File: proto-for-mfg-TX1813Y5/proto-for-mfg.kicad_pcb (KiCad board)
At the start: 2 copper layers, 191.4 x 111.9 mm, 57 parts, among them J1 Conn_01x03_Pin

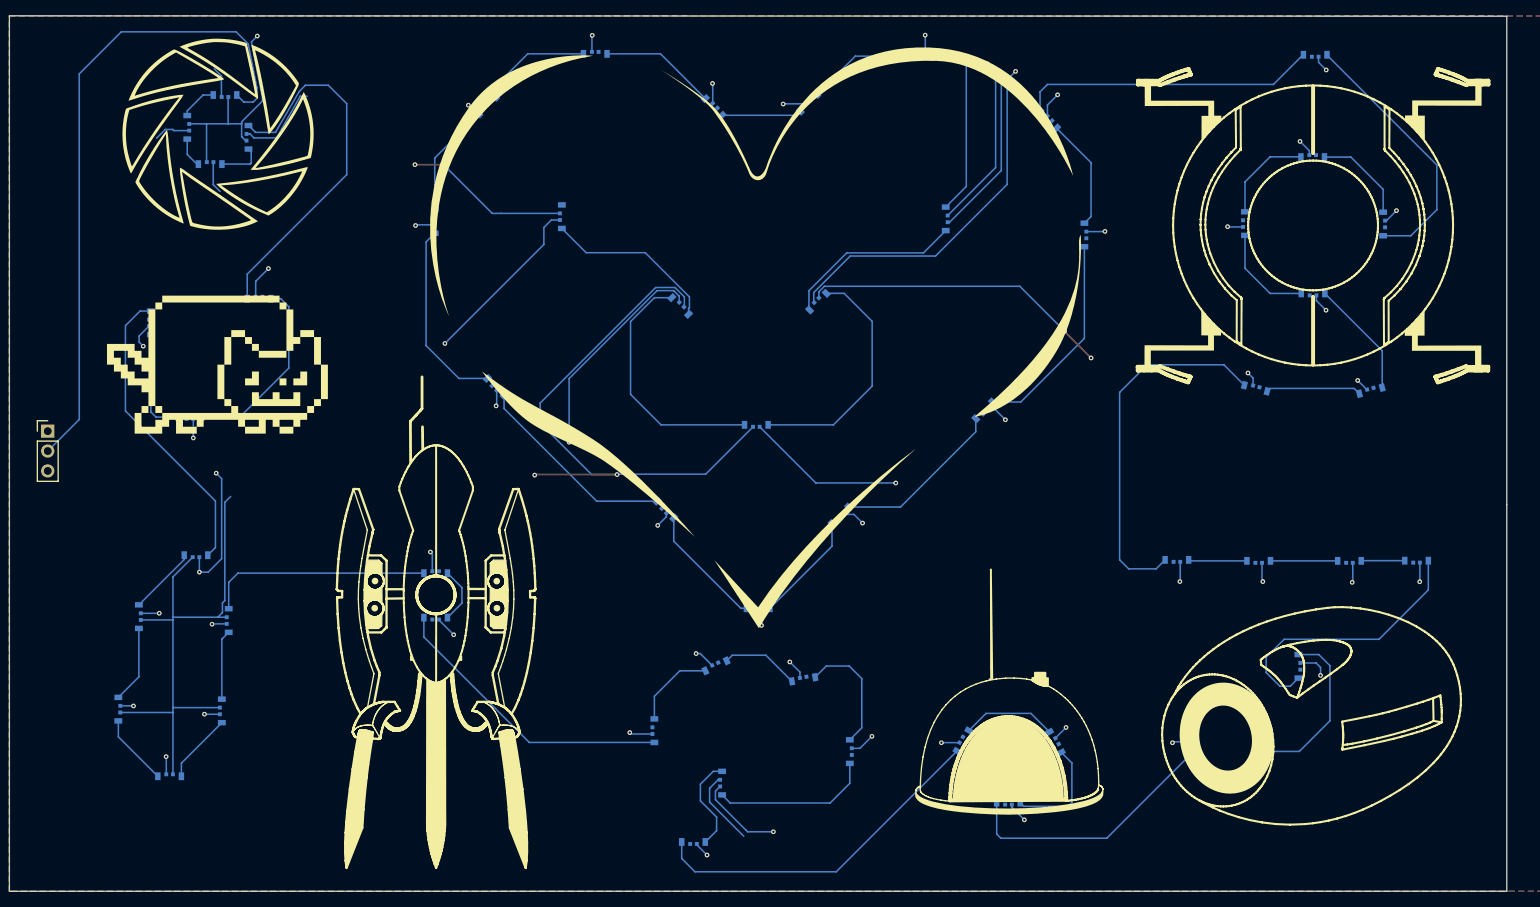
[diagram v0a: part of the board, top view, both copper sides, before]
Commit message: move over to new LED and fix design
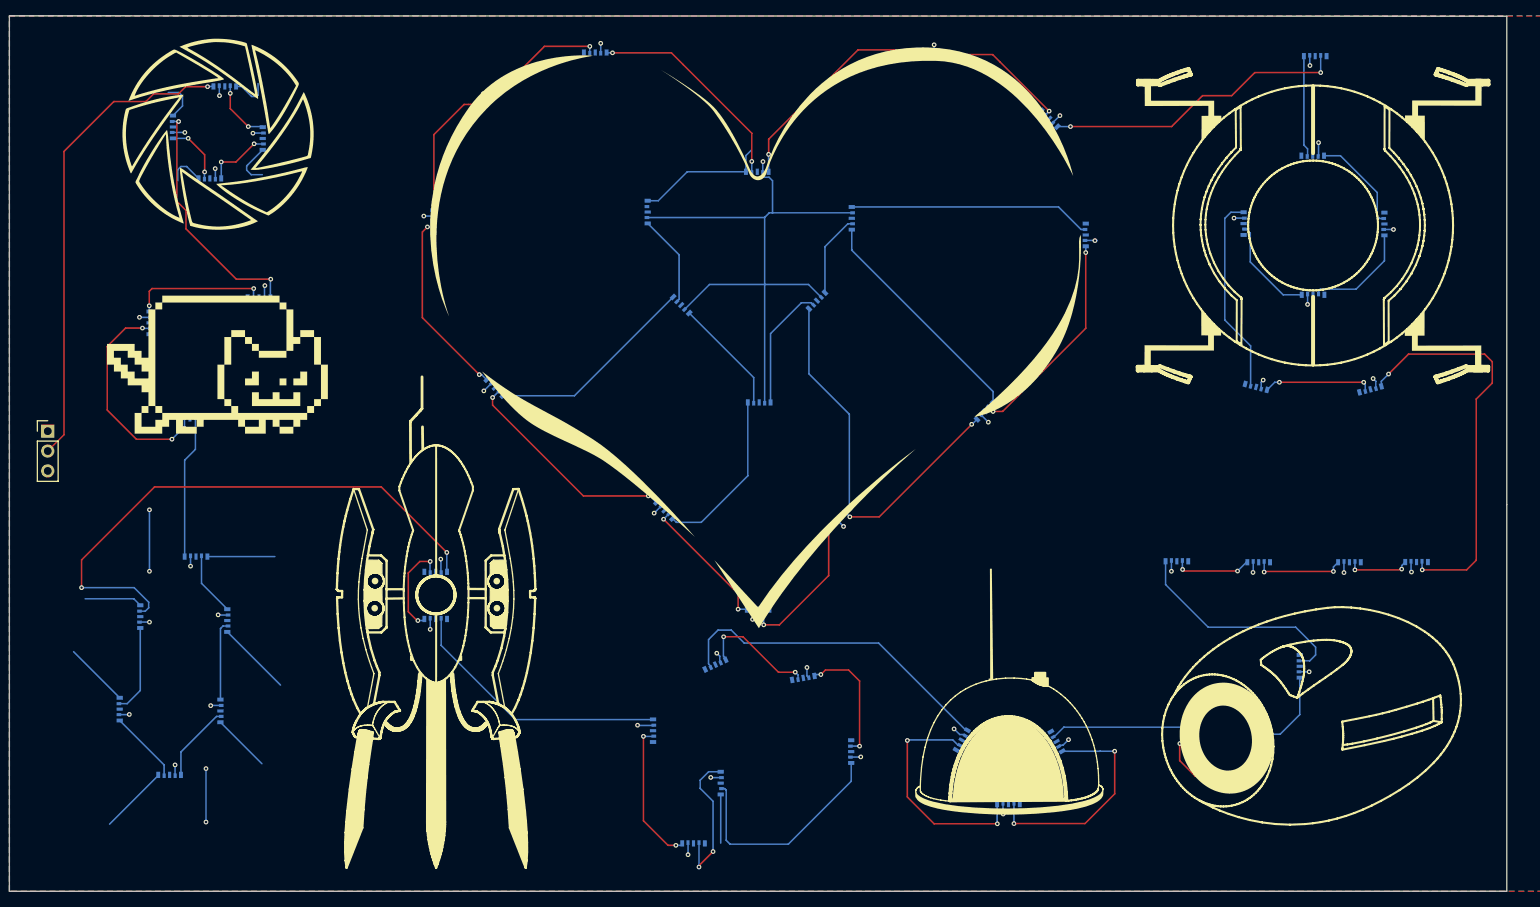
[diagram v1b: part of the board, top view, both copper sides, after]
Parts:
- removed the U50 at (124.6, 49.0)
- U1, U11, U14, U15, U16, U19, U22, U25, U26, U27, U3, U38, U39, U45, U5, U8: footprint LED_SMD:LED-SMD_4P_SK6812D-EC3210R -> LED_SMD:LED-SMD_5P-L3.2-W1.4_TX1813Y5
- U10: renamed from U12; footprint LED_SMD:LED-SMD_4P_SK6812D-EC3210R -> LED_SMD:LED-SMD_5P-L3.2-W1.4_TX1813Y5
- U12: renamed from U10; footprint LED_SMD:LED-SMD_4P_SK6812D-EC3210R -> LED_SMD:LED-SMD_5P-L3.2-W1.4_TX1813Y5
- U13: renamed from U9; footprint LED_SMD:LED-SMD_4P_SK6812D-EC3210R -> LED_SMD:LED-SMD_5P-L3.2-W1.4_TX1813Y5
- U17: renamed from U21; footprint LED_SMD:LED-SMD_4P_SK6812D-EC3210R -> LED_SMD:LED-SMD_5P-L3.2-W1.4_TX1813Y5
- U18: renamed from U20; footprint LED_SMD:LED-SMD_4P_SK6812D-EC3210R -> LED_SMD:LED-SMD_5P-L3.2-W1.4_TX1813Y5
- U2: renamed from U4; footprint LED_SMD:LED-SMD_4P_SK6812D-EC3210R -> LED_SMD:LED-SMD_5P-L3.2-W1.4_TX1813Y5
- U20: renamed from U18; footprint LED_SMD:LED-SMD_4P_SK6812D-EC3210R -> LED_SMD:LED-SMD_5P-L3.2-W1.4_TX1813Y5
- U21: renamed from U17; footprint LED_SMD:LED-SMD_4P_SK6812D-EC3210R -> LED_SMD:LED-SMD_5P-L3.2-W1.4_TX1813Y5
- U23: renamed from U24; footprint LED_SMD:LED-SMD_4P_SK6812D-EC3210R -> LED_SMD:LED-SMD_5P-L3.2-W1.4_TX1813Y5
- U24: renamed from U23; footprint LED_SMD:LED-SMD_4P_SK6812D-EC3210R -> LED_SMD:LED-SMD_5P-L3.2-W1.4_TX1813Y5
- U28: renamed from U31; footprint LED_SMD:LED-SMD_4P_SK6812D-EC3210R -> LED_SMD:LED-SMD_5P-L3.2-W1.4_TX1813Y5
- U29: renamed from U30; footprint LED_SMD:LED-SMD_4P_SK6812D-EC3210R -> LED_SMD:LED-SMD_5P-L3.2-W1.4_TX1813Y5
- U30: renamed from U29; footprint LED_SMD:LED-SMD_4P_SK6812D-EC3210R -> LED_SMD:LED-SMD_5P-L3.2-W1.4_TX1813Y5
- U31: renamed from U28; footprint LED_SMD:LED-SMD_4P_SK6812D-EC3210R -> LED_SMD:LED-SMD_5P-L3.2-W1.4_TX1813Y5
- U32: renamed from U33; footprint LED_SMD:LED-SMD_4P_SK6812D-EC3210R -> LED_SMD:LED-SMD_5P-L3.2-W1.4_TX1813Y5
- U33: renamed from U32; footprint LED_SMD:LED-SMD_4P_SK6812D-EC3210R -> LED_SMD:LED-SMD_5P-L3.2-W1.4_TX1813Y5
- U34: renamed from U35; footprint LED_SMD:LED-SMD_4P_SK6812D-EC3210R -> LED_SMD:LED-SMD_5P-L3.2-W1.4_TX1813Y5
- U35: renamed from U34; footprint LED_SMD:LED-SMD_4P_SK6812D-EC3210R -> LED_SMD:LED-SMD_5P-L3.2-W1.4_TX1813Y5
- U36: renamed from U37; footprint LED_SMD:LED-SMD_4P_SK6812D-EC3210R -> LED_SMD:LED-SMD_5P-L3.2-W1.4_TX1813Y5
- U37: renamed from U36; footprint LED_SMD:LED-SMD_4P_SK6812D-EC3210R -> LED_SMD:LED-SMD_5P-L3.2-W1.4_TX1813Y5
- U4: renamed from U2; footprint LED_SMD:LED-SMD_4P_SK6812D-EC3210R -> LED_SMD:LED-SMD_5P-L3.2-W1.4_TX1813Y5
- U40: renamed from U51; footprint LED_SMD:LED-SMD_4P_SK6812D-EC3210R -> LED_SMD:LED-SMD_5P-L3.2-W1.4_TX1813Y5
- U41: renamed from U49; footprint LED_SMD:LED-SMD_4P_SK6812D-EC3210R -> LED_SMD:LED-SMD_5P-L3.2-W1.4_TX1813Y5
- U42: renamed from U48; footprint LED_SMD:LED-SMD_4P_SK6812D-EC3210R -> LED_SMD:LED-SMD_5P-L3.2-W1.4_TX1813Y5
- U43: renamed from U47; footprint LED_SMD:LED-SMD_4P_SK6812D-EC3210R -> LED_SMD:LED-SMD_5P-L3.2-W1.4_TX1813Y5
- U44: renamed from U46; footprint LED_SMD:LED-SMD_4P_SK6812D-EC3210R -> LED_SMD:LED-SMD_5P-L3.2-W1.4_TX1813Y5
- U46: renamed from U44; footprint LED_SMD:LED-SMD_4P_SK6812D-EC3210R -> LED_SMD:LED-SMD_5P-L3.2-W1.4_TX1813Y5
- U47: renamed from U43; footprint LED_SMD:LED-SMD_4P_SK6812D-EC3210R -> LED_SMD:LED-SMD_5P-L3.2-W1.4_TX1813Y5
- U48: renamed from U42; footprint LED_SMD:LED-SMD_4P_SK6812D-EC3210R -> LED_SMD:LED-SMD_5P-L3.2-W1.4_TX1813Y5
- U49: renamed from U41; footprint LED_SMD:LED-SMD_4P_SK6812D-EC3210R -> LED_SMD:LED-SMD_5P-L3.2-W1.4_TX1813Y5
- U50: renamed from U40; footprint LED_SMD:LED-SMD_4P_SK6812D-EC3210R -> LED_SMD:LED-SMD_5P-L3.2-W1.4_TX1813Y5
- U51: renamed from U52; footprint LED_SMD:LED-SMD_4P_SK6812D-EC3210R -> LED_SMD:LED-SMD_5P-L3.2-W1.4_TX1813Y5
- U52: renamed from U53; footprint LED_SMD:LED-SMD_4P_SK6812D-EC3210R -> LED_SMD:LED-SMD_5P-L3.2-W1.4_TX1813Y5
- U53: renamed from U54; footprint LED_SMD:LED-SMD_4P_SK6812D-EC3210R -> LED_SMD:LED-SMD_5P-L3.2-W1.4_TX1813Y5
- U54: renamed from U55; footprint LED_SMD:LED-SMD_4P_SK6812D-EC3210R -> LED_SMD:LED-SMD_5P-L3.2-W1.4_TX1813Y5
- U55: renamed from U56; footprint LED_SMD:LED-SMD_4P_SK6812D-EC3210R -> LED_SMD:LED-SMD_5P-L3.2-W1.4_TX1813Y5
- U6: renamed from U7; footprint LED_SMD:LED-SMD_4P_SK6812D-EC3210R -> LED_SMD:LED-SMD_5P-L3.2-W1.4_TX1813Y5
- U7: renamed from U6; footprint LED_SMD:LED-SMD_4P_SK6812D-EC3210R -> LED_SMD:LED-SMD_5P-L3.2-W1.4_TX1813Y5
- U9: renamed from U13; footprint LED_SMD:LED-SMD_4P_SK6812D-EC3210R -> LED_SMD:LED-SMD_5P-L3.2-W1.4_TX1813Y5
- moved U51 12.1 mm to (130.3, 63.9)
- moved U55 11.1 mm to (104.1, 63.1)
- moved U41 10.0 mm to (118.1, 58.0), turned to 0 degrees
- moved U53 2.96 mm to (118.4, 87.4)
- moved U3 2.01 mm to (48.2, 58.8), turned to 0 degrees
- moved U4 2.01 mm to (43.4, 52.2), turned to -90 degrees
- moved U2 2.00 mm to (55.0, 53.7), turned to 90 degrees
- moved U1 1.27 mm to (50.1, 47.0), turned to 180 degrees
- turned U10 to 90 degrees
- turned U11 to 0 degrees
- turned U12 to -90 degrees
- turned U13 to -90 degrees
- turned U14 to 0 degrees
- turned U15 to 180 degrees
- turned U16 to 90 degrees
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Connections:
- U1 pad 1: GND -> Net-(J1-Pin_2)
- U1 pad 2: Net-(U1-DOUT) -> +3V3
- U1 pad 3: Net-(J1-Pin_2) -> unconnected-(U1-FDIN-Pad3)
- U1 pad 4: +3V3 -> Net-(U1-DO)
- U10 pad 1: GND -> Net-(U10-DIN)
- U10 pad 2: Net-(U12-DOUT) -> +3V3
- U10 pad 3: Net-(U11-DOUT) -> unconnected-(U10-FDIN-Pad3)
- U10 pad 4: +3V3 -> Net-(U10-DO)
- U11 pad 1: GND -> Net-(U10-DO)
- U11 pad 2: Net-(U11-DOUT) -> +3V3
- U11 pad 3: Net-(U10-DOUT) -> unconnected-(U11-FDIN-Pad3)
- U11 pad 4: +3V3 -> Net-(U11-DO)
- U12 pad 1: GND -> Net-(U11-DO)
- U12 pad 2: Net-(U10-DOUT) -> +3V3
- U12 pad 3: Net-(U10-DIN) -> unconnected-(U12-FDIN-Pad3)
- U12 pad 4: +3V3 -> Net-(U12-DO)
- U13 pad 1: GND -> Net-(U12-DO)
- U13 pad 2: Net-(U10-DIN) -> +3V3
- U13 pad 3: Net-(U8-DOUT) -> unconnected-(U13-FDIN-Pad3)
- U13 pad 4: +3V3 -> Net-(U13-DO)
- U14 pad 1: GND -> Net-(U13-DO)
- U14 pad 2: Net-(U14-DOUT) -> +3V3
- U14 pad 3: Net-(U13-DOUT) -> unconnected-(U14-FDIN-Pad3)
- U14 pad 4: +3V3 -> Net-(U14-DO)
- U15 pad 1: GND -> Net-(U14-DO)
- U15 pad 2: Net-(U15-DOUT) -> +3V3
- U15 pad 3: Net-(U14-DOUT) -> unconnected-(U15-FDIN-Pad3)
- U15 pad 4: +3V3 -> Net-(U15-DO)
- U16 pad 1: GND -> Net-(U15-DO)
- U16 pad 2: Net-(U16-DOUT) -> +3V3
- U16 pad 3: Net-(U15-DOUT) -> unconnected-(U16-FDIN-Pad3)
- U16 pad 4: +3V3 -> Net-(U16-DO)
- U17 pad 1: GND -> Net-(U16-DO)
- U17 pad 2: Net-(U21-DOUT) -> +3V3
- U17 pad 3: Net-(U20-DOUT) -> unconnected-(U17-FDIN-Pad3)
- U17 pad 4: +3V3 -> Net-(U17-DO)
- U18 pad 1: GND -> Net-(U17-DO)
- U18 pad 2: Net-(U20-DOUT) -> +3V3
- U18 pad 3: Net-(U19-DOUT) -> unconnected-(U18-FDIN-Pad3)
- U18 pad 4: +3V3 -> Net-(U18-DO)
- U19 pad 1: GND -> Net-(U18-DO)
- U19 pad 2: Net-(U19-DOUT) -> +3V3
- U19 pad 3: Net-(U18-DOUT) -> unconnected-(U19-FDIN-Pad3)
- U19 pad 4: +3V3 -> Net-(U19-DO)
- U2 pad 1: GND -> Net-(U1-DO)
- U2 pad 2: Net-(U4-DOUT) -> +3V3
- U2 pad 3: Net-(U3-DOUT) -> unconnected-(U2-FDIN-Pad3)
- U2 pad 4: +3V3 -> Net-(U2-DO)
- U20 pad 1: GND -> Net-(U19-DO)
- U20 pad 2: Net-(U18-DOUT) -> +3V3
- U20 pad 3: Net-(U17-DOUT) -> unconnected-(U20-FDIN-Pad3)
- U20 pad 4: +3V3 -> Net-(U20-DO)
- U21 pad 1: GND -> Net-(U20-DO)
- U21 pad 2: Net-(U17-DOUT) -> +3V3
- U21 pad 3: Net-(U16-DOUT) -> unconnected-(U21-FDIN-Pad3)
- U21 pad 4: +3V3 -> Net-(U21-DO)
- U22 pad 1: GND -> Net-(U21-DO)
- U22 pad 2: Net-(U22-DOUT) -> +3V3
- U22 pad 3: Net-(U21-DOUT) -> unconnected-(U22-FDIN-Pad3)
- U22 pad 4: +3V3 -> Net-(U22-DO)
- U23 pad 1: GND -> Net-(U22-DO)
- U23 pad 2: Net-(U24-DOUT) -> +3V3
- U23 pad 3: Net-(U23-DOUT) -> unconnected-(U23-FDIN-Pad3)
- U23 pad 4: +3V3 -> Net-(U23-DO)
- U24 pad 1: GND -> Net-(U23-DO)
- U24 pad 2: Net-(U23-DOUT) -> +3V3
- U24 pad 3: Net-(U22-DOUT) -> unconnected-(U24-FDIN-Pad3)
- U24 pad 4: +3V3 -> Net-(U24-DO)
- U25 pad 1: GND -> Net-(U24-DO)
- U25 pad 2: Net-(U25-DOUT) -> +3V3
- U25 pad 3: Net-(U24-DOUT) -> unconnected-(U25-FDIN-Pad3)
- U25 pad 4: +3V3 -> Net-(U25-DO)
- U26 pad 1: GND -> Net-(U25-DO)
- U26 pad 2: Net-(U26-DOUT) -> +3V3
- U26 pad 3: Net-(U25-DOUT) -> unconnected-(U26-FDIN-Pad3)
- U26 pad 4: +3V3 -> Net-(U26-DO)
- U27 pad 1: GND -> Net-(U26-DO)
- U27 pad 2: Net-(U27-DOUT) -> +3V3
- U27 pad 3: Net-(U26-DOUT) -> unconnected-(U27-FDIN-Pad3)
- U27 pad 4: +3V3 -> Net-(U27-DO)
- U28 pad 1: GND -> Net-(U27-DO)
- U28 pad 2: Net-(U31-DOUT) -> +3V3
- U28 pad 3: Net-(U30-DOUT) -> unconnected-(U28-FDIN-Pad3)
- U28 pad 4: +3V3 -> Net-(U28-DO)
- U29 pad 1: GND -> Net-(U28-DO)
- U29 pad 2: Net-(U30-DOUT) -> +3V3
- U29 pad 3: Net-(U29-DOUT) -> unconnected-(U29-FDIN-Pad3)
- U29 pad 4: +3V3 -> Net-(U29-DO)
- U3 pad 1: GND -> Net-(U2-DO)
- U3 pad 2: Net-(U3-DOUT) -> +3V3
- U3 pad 3: Net-(U2-DOUT) -> unconnected-(U3-FDIN-Pad3)
- U3 pad 4: +3V3 -> Net-(U3-DO)
- U30 pad 1: GND -> Net-(U29-DO)
- U30 pad 2: Net-(U29-DOUT) -> +3V3
- U30 pad 3: Net-(U28-DOUT) -> unconnected-(U30-FDIN-Pad3)
- U30 pad 4: +3V3 -> Net-(U30-DO)
- U31 pad 1: GND -> Net-(U30-DO)
- U31 pad 2: Net-(U28-DOUT) -> +3V3
- U31 pad 3: Net-(U27-DOUT) -> unconnected-(U31-FDIN-Pad3)
- U31 pad 4: +3V3 -> Net-(U31-DO)
- U32 pad 1: GND -> Net-(U31-DO)
- U32 pad 2: Net-(U33-DOUT) -> +3V3
- U32 pad 3: Net-(U32-DOUT) -> unconnected-(U32-FDIN-Pad3)
- U32 pad 4: +3V3 -> Net-(U32-DO)
- U33 pad 1: GND -> Net-(U32-DO)
- U33 pad 2: Net-(U32-DOUT) -> +3V3
- U33 pad 3: Net-(U31-DOUT) -> unconnected-(U33-FDIN-Pad3)
- U33 pad 4: +3V3 -> Net-(U33-DO)
- U34 pad 1: GND -> Net-(U33-DO)
- U34 pad 2: Net-(U35-DOUT) -> +3V3
- U34 pad 3: Net-(U34-DOUT) -> unconnected-(U34-FDIN-Pad3)
- U34 pad 4: +3V3 -> Net-(U34-DO)
- U35 pad 1: GND -> Net-(U34-DO)
- U35 pad 2: Net-(U34-DOUT) -> +3V3
- U35 pad 3: Net-(U33-DOUT) -> unconnected-(U35-FDIN-Pad3)
- U35 pad 4: +3V3 -> Net-(U35-DO)
- U36 pad 1: GND -> Net-(U35-DO)
- U36 pad 2: Net-(U37-DOUT) -> +3V3
- U36 pad 3: Net-(U36-DOUT) -> unconnected-(U36-FDIN-Pad3)
- U36 pad 4: +3V3 -> Net-(U36-DO)
- U37 pad 1: GND -> Net-(U36-DO)
- U37 pad 2: Net-(U36-DOUT) -> +3V3
- U37 pad 3: Net-(U35-DOUT) -> unconnected-(U37-FDIN-Pad3)
- U37 pad 4: +3V3 -> Net-(U37-DO)
- U38 pad 1: GND -> Net-(U37-DO)
- U38 pad 2: Net-(U38-DOUT) -> +3V3
- U38 pad 3: Net-(U37-DOUT) -> unconnected-(U38-FDIN-Pad3)
- U38 pad 4: +3V3 -> Net-(U38-DO)
- U39 pad 1: GND -> Net-(U38-DO)
- U39 pad 2: Net-(U39-DOUT) -> +3V3
- U39 pad 3: Net-(U38-DOUT) -> unconnected-(U39-FDIN-Pad3)
- U39 pad 4: +3V3 -> Net-(U39-DO)
- U4 pad 1: GND -> Net-(U3-DO)
- U4 pad 2: Net-(U2-DOUT) -> +3V3
- U4 pad 3: Net-(U1-DOUT) -> unconnected-(U4-FDIN-Pad3)
- U4 pad 4: +3V3 -> Net-(U4-DO)
- U40 pad 1: GND -> Net-(U39-DO)
- U40 pad 2: Net-(U51-DOUT) -> +3V3
- U40 pad 3: Net-(U50-DOUT) -> unconnected-(U40-FDIN-Pad3)
- U40 pad 4: +3V3 -> Net-(U40-DO)
- U41 pad 1: GND -> Net-(U40-DO)
- U41 pad 2: Net-(U49-DOUT) -> +3V3
- U41 pad 3: Net-(U48-DOUT) -> unconnected-(U41-FDIN-Pad3)
- U41 pad 4: +3V3 -> Net-(U41-DO)
- U42 pad 1: GND -> Net-(U41-DO)
- U42 pad 2: Net-(U48-DOUT) -> +3V3
- U42 pad 3: Net-(U47-DOUT) -> unconnected-(U42-FDIN-Pad3)
- U42 pad 4: +3V3 -> Net-(U42-DO)
- U43 pad 1: GND -> Net-(U42-DO)
- U43 pad 2: Net-(U47-DOUT) -> +3V3
- U43 pad 3: Net-(U46-DOUT) -> unconnected-(U43-FDIN-Pad3)
- U43 pad 4: +3V3 -> Net-(U43-DO)
- U44 pad 1: GND -> Net-(U43-DO)
- U44 pad 2: Net-(U46-DOUT) -> +3V3
- U44 pad 3: Net-(U45-DOUT) -> unconnected-(U44-FDIN-Pad3)
- U44 pad 4: +3V3 -> Net-(U44-DO)
- U45 pad 1: GND -> Net-(U44-DO)
- U45 pad 2: Net-(U45-DOUT) -> +3V3
- U45 pad 3: Net-(U44-DOUT) -> unconnected-(U45-FDIN-Pad3)
- U45 pad 4: +3V3 -> Net-(U45-DO)
- U46 pad 1: GND -> Net-(U45-DO)
- U46 pad 2: Net-(U44-DOUT) -> +3V3
- U46 pad 3: Net-(U43-DOUT) -> unconnected-(U46-FDIN-Pad3)
- U46 pad 4: +3V3 -> Net-(U46-DO)
- U47 pad 1: GND -> Net-(U46-DO)
- U47 pad 2: Net-(U43-DOUT) -> +3V3
- U47 pad 3: Net-(U42-DOUT) -> unconnected-(U47-FDIN-Pad3)
- U47 pad 4: +3V3 -> Net-(U47-DO)
- U48 pad 1: GND -> Net-(U47-DO)
- U48 pad 2: Net-(U42-DOUT) -> +3V3
- U48 pad 3: Net-(U41-DOUT) -> unconnected-(U48-FDIN-Pad3)
- U48 pad 4: +3V3 -> Net-(U48-DO)
- U49 pad 1: GND -> Net-(U48-DO)
- U49 pad 2: Net-(U41-DOUT) -> +3V3
- U49 pad 3: Net-(U40-DOUT) -> unconnected-(U49-FDIN-Pad3)
- U49 pad 4: +3V3 -> Net-(U49-DO)
- U5 pad 1: GND -> Net-(U4-DO)
- U5 pad 2: Net-(U5-DOUT) -> +3V3
- U5 pad 3: Net-(U4-DOUT) -> unconnected-(U5-FDIN-Pad3)
- U5 pad 4: +3V3 -> Net-(U5-DO)
- U50 pad 1: GND -> Net-(U49-DO)
- U50 pad 2: Net-(U40-DOUT) -> +3V3
- U50 pad 3: Net-(U39-DOUT) -> unconnected-(U50-FDIN-Pad3)
- U50 pad 4: +3V3 -> Net-(U50-DO)
- U51 pad 1: GND -> Net-(U50-DO)
- U51 pad 2: Net-(U52-DOUT) -> +3V3
- U51 pad 3: Net-(U51-DOUT) -> unconnected-(U51-FDIN-Pad3)
- U51 pad 4: +3V3 -> Net-(U51-DO)
- U52 pad 1: GND -> Net-(U51-DO)
- U52 pad 2: Net-(U53-DOUT) -> +3V3
- U52 pad 3: Net-(U52-DOUT) -> unconnected-(U52-FDIN-Pad3)
- U52 pad 4: +3V3 -> Net-(U52-DO)
- U53 pad 1: GND -> Net-(U52-DO)
- U53 pad 2: Net-(U54-DOUT) -> +3V3
- U53 pad 3: Net-(U53-DOUT) -> unconnected-(U53-FDIN-Pad3)
- U53 pad 4: +3V3 -> Net-(U53-DO)
- U54 pad 1: GND -> Net-(U53-DO)
- U54 pad 2: Net-(U55-DOUT) -> +3V3
- U54 pad 3: Net-(U54-DOUT) -> unconnected-(U54-FDIN-Pad3)
- U54 pad 4: +3V3 -> Net-(U54-DO)
- U55 pad 1: GND -> Net-(U54-DO)
- U55 pad 2: unconnected-(U56-DOUT-Pad2) -> +3V3
- U55 pad 3: Net-(U55-DOUT) -> unconnected-(U55-FDIN-Pad3)
- U55 pad 4: +3V3 -> unconnected-(U55-DO-Pad4)
- U6 pad 1: GND -> Net-(U5-DO)
- U6 pad 2: Net-(U7-DOUT) -> +3V3
- U6 pad 3: Net-(U6-DOUT) -> unconnected-(U6-FDIN-Pad3)
- U6 pad 4: +3V3 -> Net-(U6-DO)
- U7 pad 1: GND -> Net-(U6-DO)
- U7 pad 2: Net-(U6-DOUT) -> +3V3
- U7 pad 3: Net-(U5-DOUT) -> unconnected-(U7-FDIN-Pad3)
- U7 pad 4: +3V3 -> Net-(U7-DO)
- U8 pad 1: GND -> Net-(U7-DO)
- U8 pad 2: Net-(U8-DOUT) -> +3V3
- U8 pad 3: Net-(U7-DOUT) -> unconnected-(U8-FDIN-Pad3)
- U8 pad 4: +3V3 -> Net-(U8-DO)
- U9 pad 1: GND -> Net-(U8-DO)
- U9 pad 2: Net-(U13-DOUT) -> +3V3
- U9 pad 3: Net-(U12-DOUT) -> unconnected-(U9-FDIN-Pad3)
- U9 pad 4: +3V3 -> Net-(U10-DIN)
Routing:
- net +3V3: track 307.5 -> 160.9 mm
- net Net-(U13-DO): track 0.00 -> 71.4 mm, vias 0 -> 2
- net GND: track 256.1 -> 200.1 mm, vias 6 -> 0
- net Net-(U31-DO): track 0.00 -> 51.4 mm, vias 0 -> 2
- net Net-(U4-DOUT): track 47.4 -> 0.00 mm
- net Net-(U31-DOUT): track 46.7 -> 0.00 mm
- net Net-(U21-DOUT): track 44.4 -> 0.00 mm
- net Net-(U21-DO): track 0.00 -> 42.6 mm
- net Net-(U38-DO): track 0.00 -> 38.7 mm, vias 0 -> 2
- net Net-(U7-DOUT): track 38.5 -> 0.00 mm
- net Net-(U38-DOUT): track 38.1 -> 0.00 mm
- net Net-(U15-DOUT): track 37.5 -> 0.00 mm
- net Net-(U27-DOUT): track 35.3 -> 0.00 mm
- net Net-(U15-DO): track 0.00 -> 34.5 mm
- net Net-(U24-DOUT): track 34.2 -> 0.00 mm
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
